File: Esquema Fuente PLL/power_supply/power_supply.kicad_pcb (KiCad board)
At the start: 2 copper layers, 96 x 73 mm, 6 parts, among them J1 Terminal_01x02, J6 Barrel_Jack_Switch, J7 Terminal_01x02

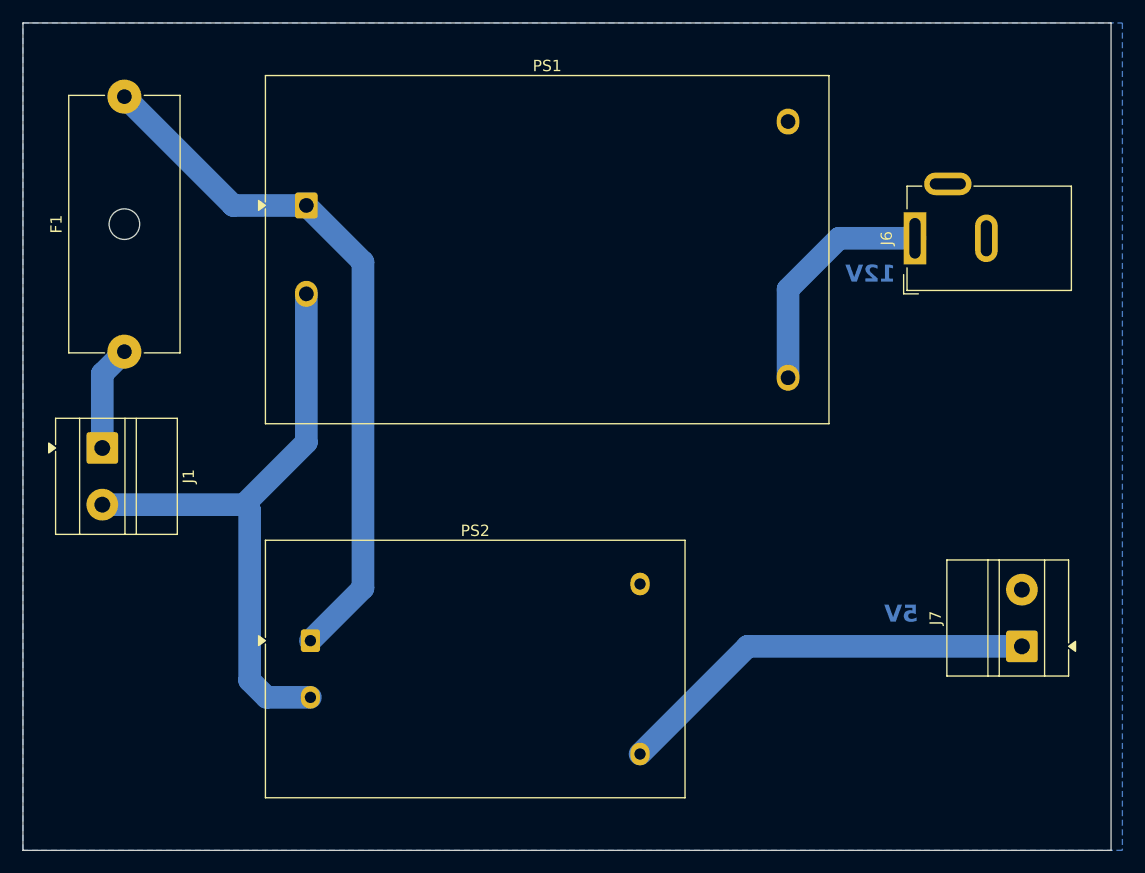
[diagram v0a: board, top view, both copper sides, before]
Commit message: se realizaron cambios en el esquema, se agrega un varistor y se hace una div entre parte fria y caliente
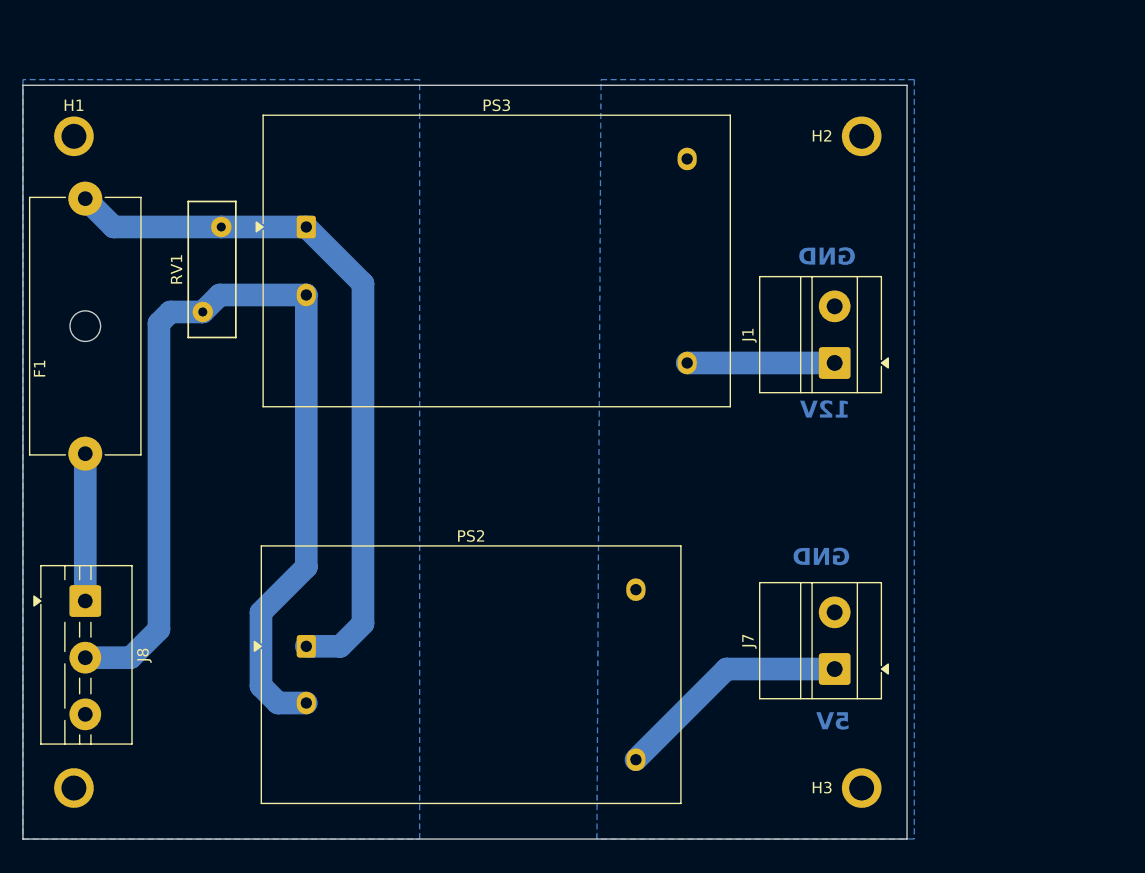
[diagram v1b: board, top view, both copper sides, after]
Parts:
- removed J6: Barrel_Jack_Switch, Connector_BarrelJack:BarrelJack_GCT_DCJ200-10-A_Horizontal
- removed PS1: HLK-10M12, Converter_ACDC:Converter_ACDC_Hi-Link_HLK-10Mxx
- added H1: MountingHole_2.2mm_M2_ISO7380_Pad, MountingHole:MountingHole_2.2mm_M2_ISO7380_Pad, F.Cu at (89.5, 71.0)
- added H2: MountingHole_2.2mm_M2_ISO7380_Pad, MountingHole:MountingHole_2.2mm_M2_ISO7380_Pad, F.Cu at (159.0, 71.0)
- added H3: MountingHole_2.2mm_M2_ISO7380_Pad, MountingHole:MountingHole_2.2mm_M2_ISO7380_Pad, F.Cu at (159.0, 128.5)
- added H4: MountingHole_2.2mm_M2_ISO7380_Pad, MountingHole:MountingHole_2.2mm_M2_ISO7380_Pad, B.Cu at (89.5, 128.5)
- added J8: Terminal_01x03, TerminalBlock:TerminalBlock_MaiXu_MX126-5.0-03P_1x03_P5.00mm, F.Cu at (90.5, 112.0)
- added PS3: HLK-5M12, Converter_ACDC:Converter_ACDC_Hi-Link_HLK-5Mxx, F.Cu at (110.0, 79.0)
- added RV1: Varistor, Varistor:RV_Disc_D12mm_W4.2mm_P7.5mm, F.Cu at (102.5, 79.0)
- moved J1 65.1 mm to (156.6, 91.0), turned to 90 degrees
- moved J7 16.6 mm to (156.6, 118.0)
- moved F1 9.64 mm to (90.5, 99.0)
- moved PS2 0.62 mm to (110.0, 116.0)
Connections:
- F1 pad 1: Net-(J1-Pin_1) -> Net-(J8-Pin_1)
- J1 pad 1: Net-(J1-Pin_1) -> +12V
- J1 pad 2: Net-(J1-Pin_2) -> GND
- PS2 pad 2: Net-(J1-Pin_2) -> Net-(J8-Pin_2)
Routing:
- net Net-(J8-Pin_2): track 0.00 -> 89.3 mm
- net Net-(J1-Pin_2): track 55.1 -> 0.00 mm
- net +5V: track 37.6 -> 20.9 mm
- net Net-(J8-Pin_1): track 0.00 -> 13.0 mm
- net Net-(J1-Pin_1): track 9.31 -> 0.00 mm
- net +12V: track 20.9 -> 13.0 mm
- net Net-(PS2-AC/L): track 62.4 -> 63.4 mm
- added copper zone on B.Cu, net Earth
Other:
- board size 96 x 73 mm -> 78 x 66.5 mm
- board text added: "GND"
